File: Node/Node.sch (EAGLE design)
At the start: 28 parts, among them IC1 4050D, IC2 LP298XS, IC3 DS3231/SO, M2 WIRELESS-NRF24L01-PA-EXT, U2 ATMEGA328P-PU, X1 MICROSD

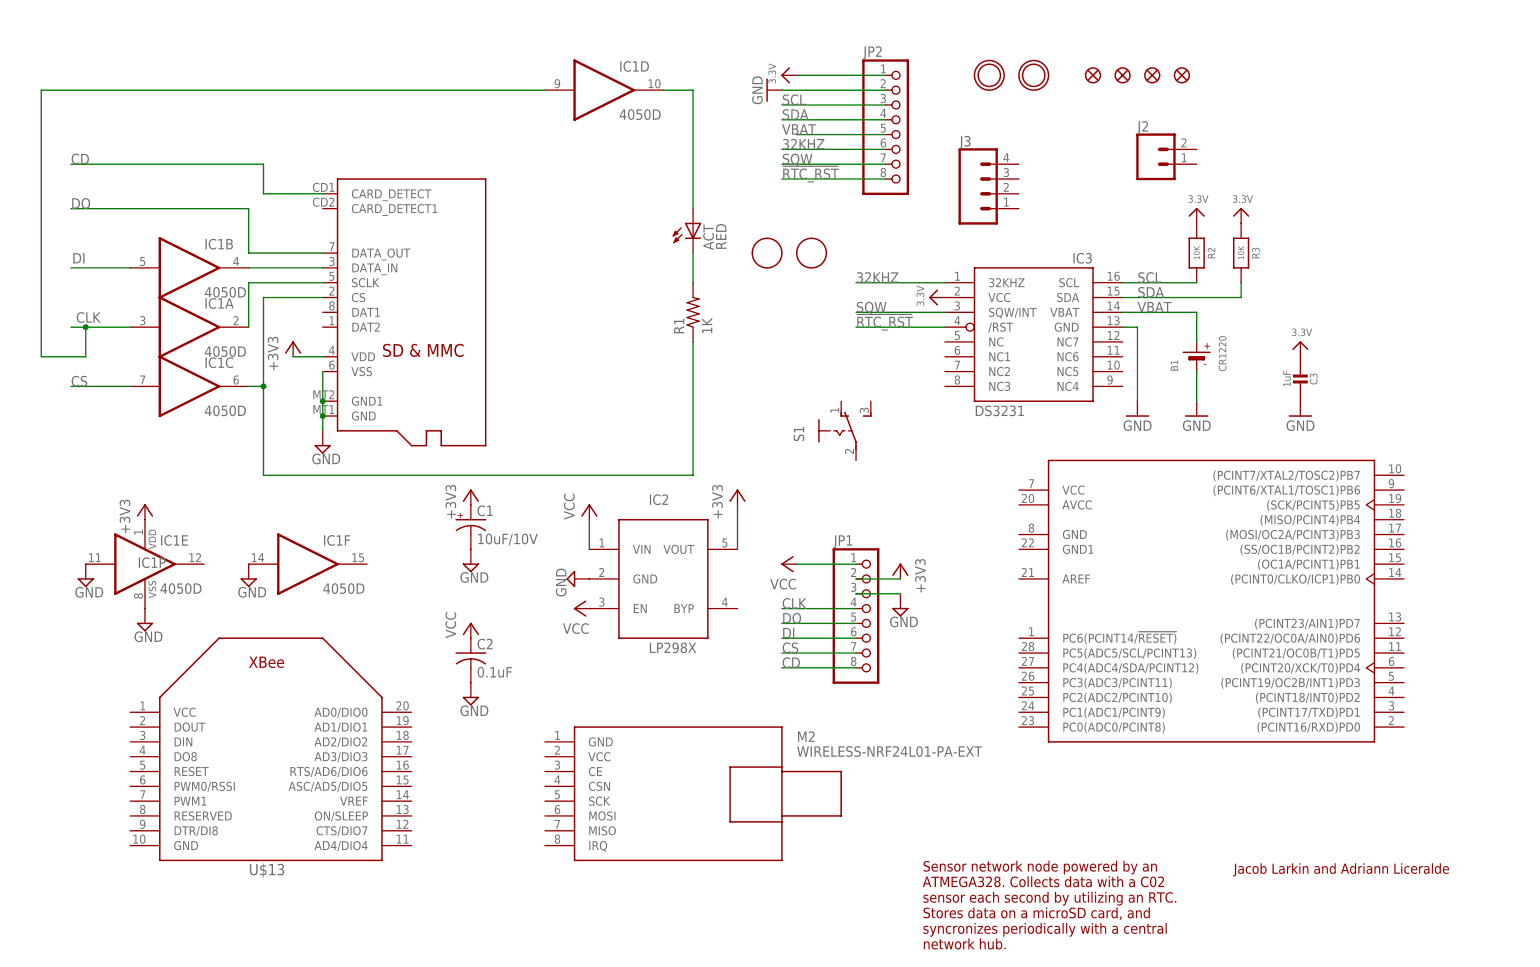
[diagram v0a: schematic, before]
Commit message: Added some connections to Node schematic
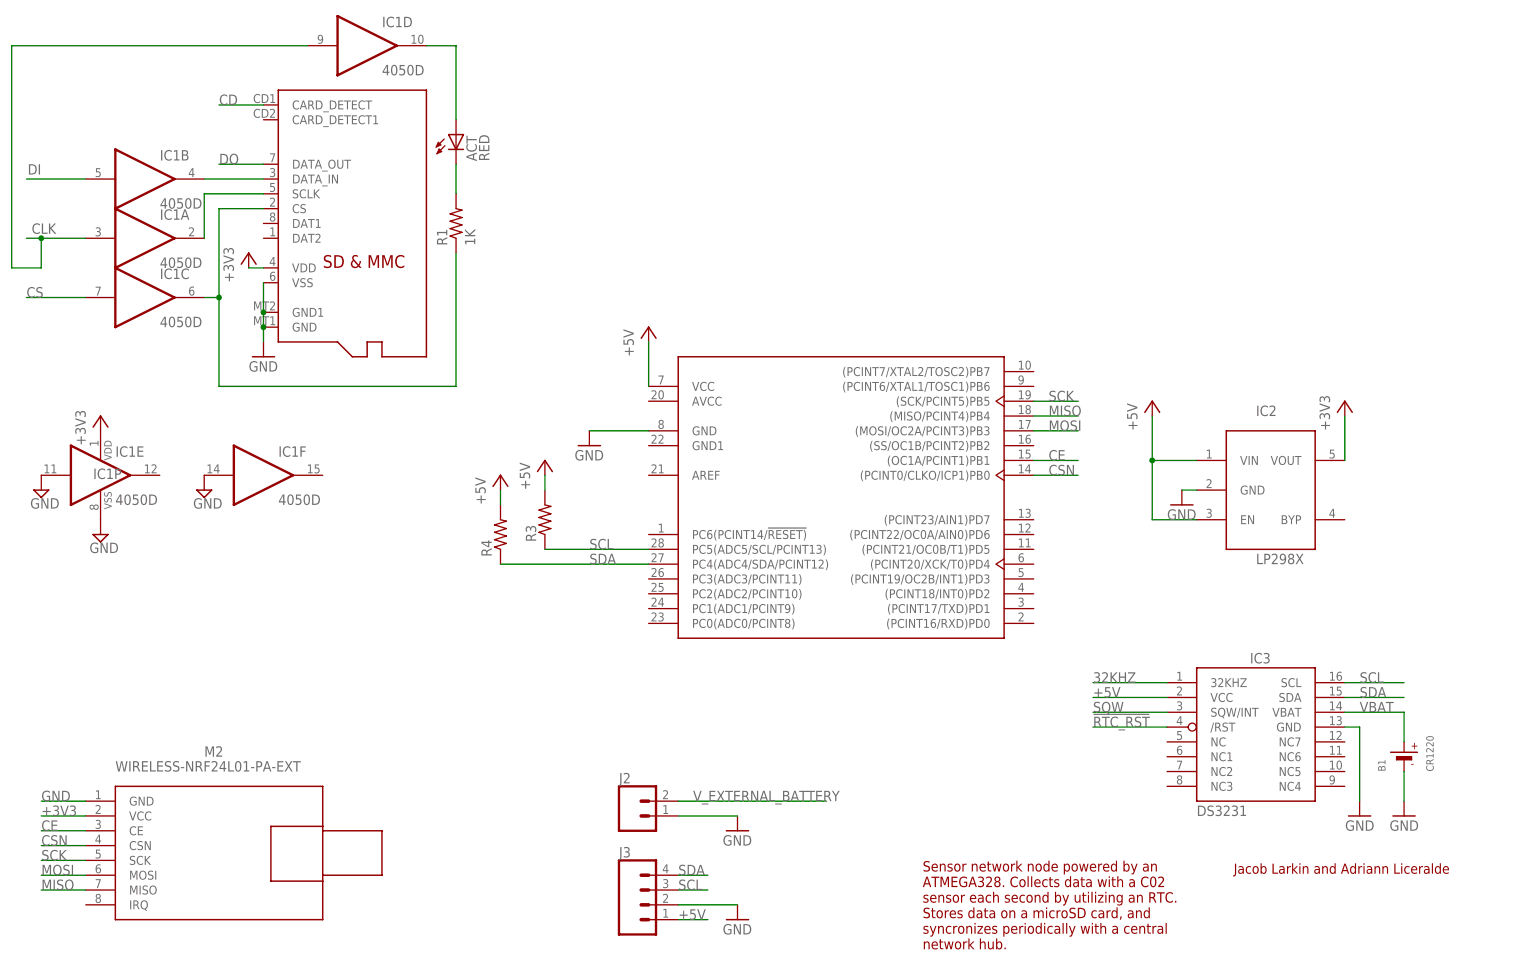
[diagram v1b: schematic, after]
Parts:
- removed C1: 10uF/10V, adafruit:CPOL-USA/3216-18R
- removed C2: 0.1uF, adafruit:C-USC0805K
- removed C3: 1uF, microbuilder:CAP_CERAMIC0805-NOOUTLINE
- removed FID1, FID2, FID3, FID4: FIDUCIAL"", microbuilder:FIDUCIAL""
- removed JP1: (no value), adafruit:PINHD-1X8BIG
- removed JP2: (no value), microbuilder:HEADER-1X870MIL
- removed R2: 10K, microbuilder:RESISTOR0805_NOOUTLINE
- removed S1: (no value), switch:255SB
- removed U$1, U$2: FIDUCIAL, adafruit:FIDUCIAL
- removed U$13: XBEE, adafruit:XBEE
- removed U$7, U$8: MOUNTINGHOLE2.5, microbuilder:MOUNTINGHOLE2.5
- added R4: (no value), rcl:R-US_R0805
- R3: value 10K -> (none); device microbuilder:RESISTOR0805_NOOUTLINE -> rcl:R-US_R0805
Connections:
- removed net 3.3V: C3.2, IC3.VCC, JP2.1, R2.1, R3.1
- removed net GND_RTC: B1.-, C3.1, IC3.GND, JP2.2
- removed net VCC_SD: C2.1, IC2.EN, IC2.VIN, JP1.1
- new net +5V: IC2.EN, IC2.VIN, IC3.VCC, J3.1, R3.2, R4.2, U2.VCC
- new net CE: M2.CE, U2.(OC1A/PCINT1)PB1
- new net CSN: M2.CSN, U2.(PCINT0/CLKO/ICP1)PB0
- new net GND: B1.-, IC2.GND, IC3.GND, J2.1, J3.2, M2.GND, U2.GND, X1.GND, X1.GND1, X1.VSS
- new net MISO: M2.MISO, U2.(MISO/PCINT4)PB4
- new net MOSI: M2.MOSI, U2.(MOSI/OC2A/PCINT3)PB3
- new net SCK: M2.SCK, U2.(SCK/PCINT5)PB5
- new net V_EXTERNAL_BATTERY: J2.2
- net !RTC_RST: no longer JP2.8
- net +3V3: now also M2.VCC; no longer C1.+, JP1.2
- net 32KHZ: no longer JP2.6
- net CD: no longer JP1.8
- net CLK: no longer JP1.4
- net CS: no longer JP1.7
- net DI: no longer JP1.6
- net DO: no longer JP1.5
- net GND_SD: no longer C1.-, C2.2, IC2.GND, JP1.3, X1.GND, X1.GND1, X1.VSS
- net SCL: now also J3.3, R3.1, U2.PC5(ADC5/SCL/PCINT13); no longer JP2.3, R2.2
- net SDA: now also J3.4, R4.1, U2.PC4(ADC4/SDA/PCINT12); no longer JP2.4, R3.2
- net SQW: no longer JP2.7
- net VBAT: no longer JP2.5
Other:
- moved on the sheet: ACT, B1, IC1A, IC1B, IC1C, IC1D, IC1E, IC1F, IC1P, IC2, IC3, J2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
